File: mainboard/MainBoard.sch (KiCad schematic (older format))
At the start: 37 parts, among them J1 CONN_1x4, J2 CONN_2X3, J3 CONN_2X3, J5 SWDEBUG_CONNECTOR, J7 CONN_2X12, U1 Tex_DCDC

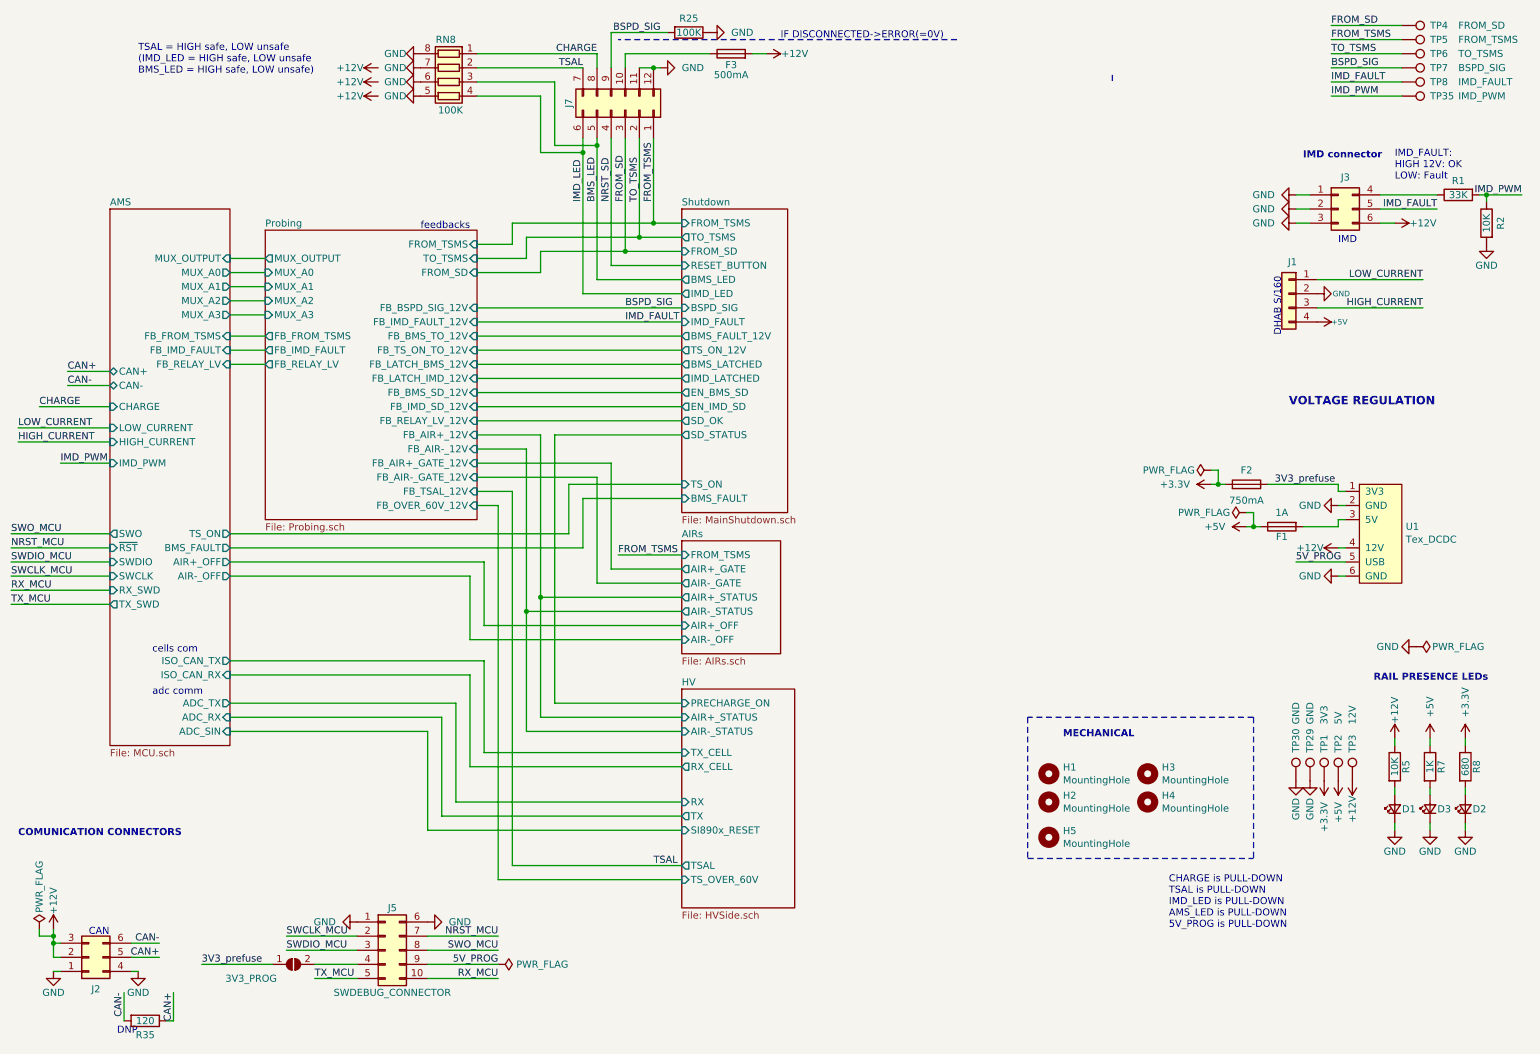
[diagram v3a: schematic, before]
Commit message: Renamed handcart detection
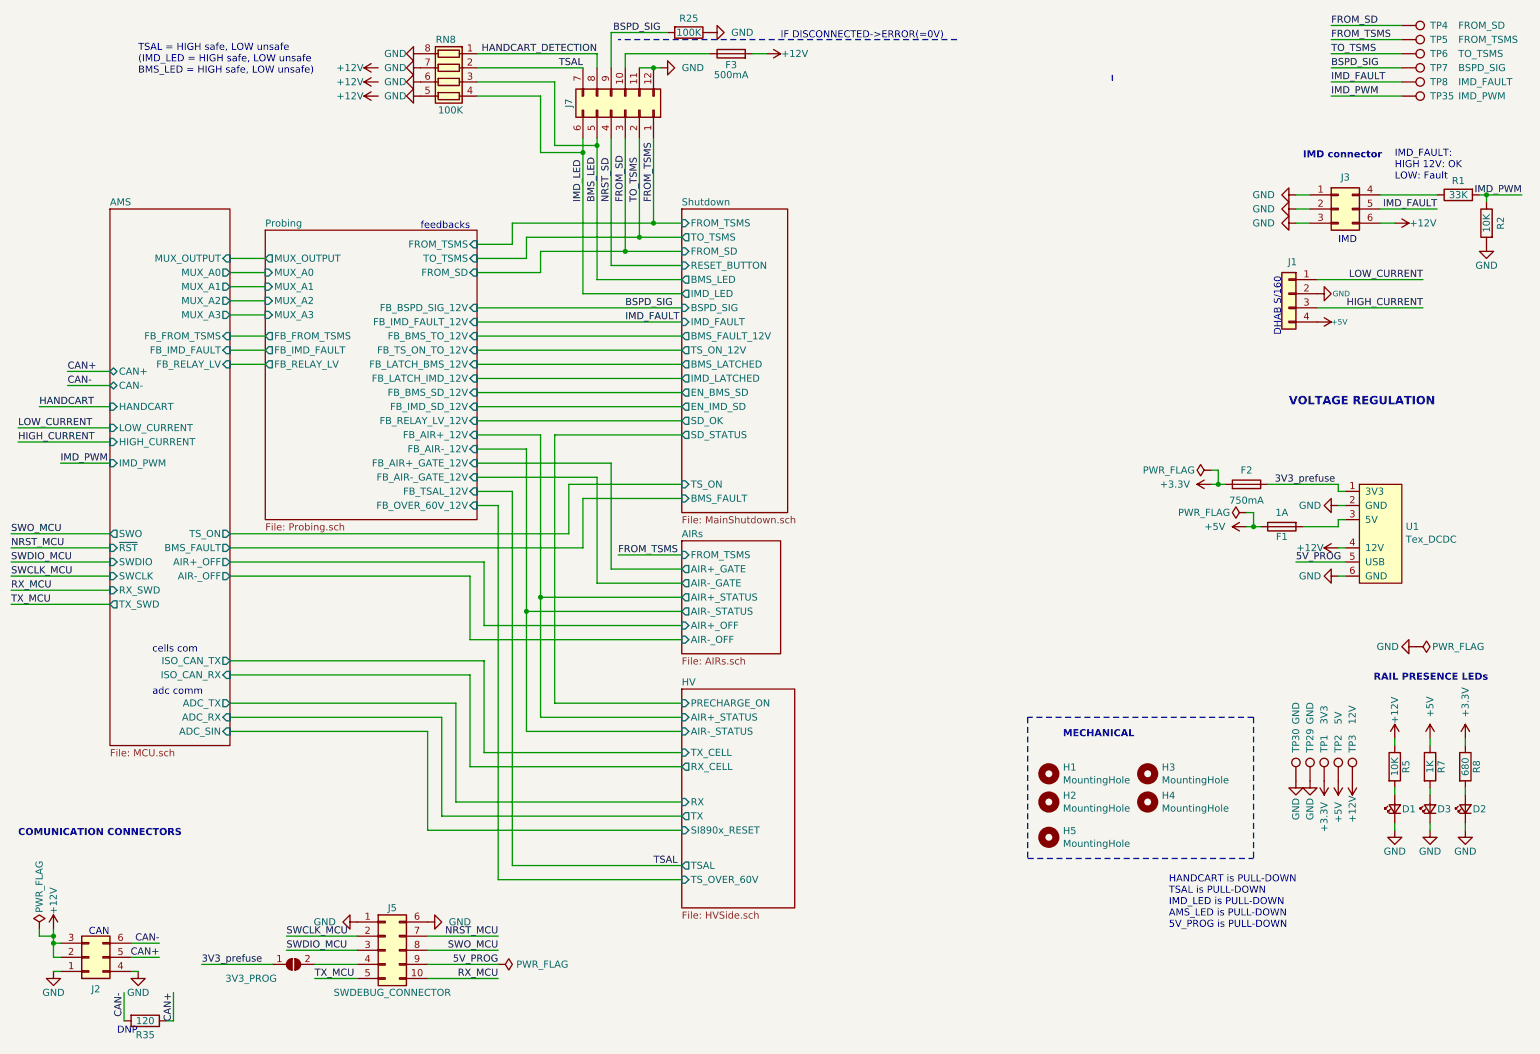
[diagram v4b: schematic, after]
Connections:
- net CHARGE renamed HANDCART_DETECTION
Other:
- note added: "HANDCART is PULL-DOWN\nTSAL is PULL-DOWN\nIMD_LED is PULL-DOWN\nAMS_LED is PULL-DOWN\n5V_PROG is PULL-DOWN"
- note removed: "CHARGE is PULL-DOWN\nTSAL is PULL-DOWN\nIMD_LED is PULL-DOWN\nAMS_LED is PULL-DOWN\n5V_PROG is PULL-DOWN"
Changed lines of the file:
@@
 F2 "HIGH_CURRENT" I L 1200 3550 50
 F3 "LOW_CURRENT" I L 1200 3450 50
-F4 "CHARGE" I L 1200 3300 50
+F4 "HANDCART" I L 1200 3300 50
 F5 "SWDIO" I L 1200 4400 50
 F6 "SWCLK" I L 1200 4500 50
@@
 BSPD_SIG
 Text Notes 8700 7000 0    50   ~ 0
-CHARGE is PULL-DOWN\nTSAL is PULL-DOWN\nIMD_LED is PULL-DOWN\nAMS_LED is PULL-DOWN\n5V_PROG is PULL-DOWN
+HANDCART is PULL-DOWN\nTSAL is PULL-DOWN\nIMD_LED is PULL-DOWN\nAMS_LED is PULL-DOWN\n5V_PROG is PULL-DOWN
 Text Label 4850 2700 0    50   ~ 0
 IMD_FAULT
@@
 	4950 1400 4950 2100
 Text Label 700  3300 0    50   ~ 0
-CHARGE
+HANDCART
 Wire Wire Line
 	700  3300 1200 3300
@@
 IMD_PWM
 Text Label 4650 800  2    50   ~ 0
-CHARGE
+HANDCART_DETECTION
 Wire Wire Line
 	5050 900  5100 900

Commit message: Correction almost finished, Started layouting
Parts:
- removed J1: CONN_1x4, MainBoard:Molex_Micro-Fit_3.0_43650-0415_1x04_P3.00mm_Vertical, symbol Connector_Generic:Conn_01x04
- removed R25: 100K, Resistor_SMD:R_0603_1608Metric, symbol Device:R
- removed R35: 120, Resistor_SMD:R_0805_2012Metric, symbol Device:R
- H1, H2, H3, H4, H5: footprint MountingHole:MountingHole_3mm -> Eagle_Main:MountingHole_3.2_6.1Free
- J2: value CONN_2X3 -> CAN_POWER; footprint MainBoard:Molex_Micro-Fit_3.0_43045-0612_2x03_P3.00mm_Vertical -> Connector_Molex:Molex_Micro-Fit_3.0_43045-0612_2x03_P3.00mm_Vertical
- J3: footprint MainBoard:Molex_Micro-Fit_3.0_43045-0612_2x03_P3.00mm_Vertical -> Connector_Molex:Molex_Micro-Fit_3.0_43045-0612_2x03_P3.00mm_Vertical
- J7: value CONN_2X12 -> SIGNALS_INOUT; footprint MainBoard:Molex_Micro-Fit_3.0_43045-1212_2x06_P3.00mm_Vertical -> Connector_Molex:Molex_Micro-Fit_3.0_43045-1212_2x06_P3.00mm_Vertical; symbol Connector_Generic:Conn_02x06_Counter_Clockwise -> Connector_Generic:Conn_02x06_Top_Bottom
- RN8: footprint MainBoard:R_network_4x1_bourns_CAY16 -> Resistor_SMD:R_Array_Convex_4x0603
- TP29, TP30: footprint MainBoard:TestPoint_GNDedge -> Eagle_Main:TestPoint_GNDedge
- TP4: value FROM_SD -> SD_IN
- TP5: value FROM_TSMS -> SD_END
- TP6: value TO_TSMS -> SD_OUT
- TP7: value BSPD_SIG -> EXT_FAULT
- U1: footprint MainBoard:Tex_DCDC_vertical -> Eagle_Main:Tex_DCDC_vertical_up; symbol MainBoard:Tex_DCDC -> Eagle_Main:Tex_DCDC
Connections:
- net GND: now also J7.7 (Pin_7), J7.8 (Pin_8); no longer J7.11 (Pin_11), J7.12 (Pin_12)
- net HANDCART_DETECTION: now also J7.9 (Pin_9); no longer J7.8 (Pin_8)
- net TSAL: now also J7.11 (Pin_11); no longer J7.7 (Pin_7)
- net EXT_FAULT: now reaches J7.10 (Pin_10)
- net EXT_FAULT: now also TP7.1; no longer F3.1
- net BMS_LED renamed BMS_COCKPIT
- net BMS_COCKPIT: now also RN8.4 (R4.1); no longer RN8.3 (R3.1)
- removed net BSPD_SIG: J7.9 (Pin_9), TP7.1
- net FROM_SD renamed SD_IN
- net FROM_TSMS renamed SD_END
- net IMD_LED renamed IMD_COCKPIT
- net IMD_COCKPIT: now also RN8.3 (R3.1); no longer RN8.4 (R4.1)
- net NRST_SD renamed SD_RESET
- net TO_TSMS renamed SD_OUT
- new net TSAL_12V: F3.1, J7.12 (Pin_12)
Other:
- note added: "HANDCART is PULL-DOWN\nTSAL is PULL-DOWN\nIMD_COCKPIT is PULL-DOWN\nAMS_LED is PULL-DOWN\n5V_PROG is PULL-DOWN"
- note added: "TSAL = HIGH safe, LOW unsafe\n(IMD_COCKPIT = HIGH safe, LOW fault\nBMS_COCKPIT = HIGH safe, LOW fault)"
- note removed: "CAN"
- note removed: "DHAB S/160"
- note removed: "DNP"
- note removed: "HANDCART is PULL-DOWN\nTSAL is PULL-DOWN\nIMD_LED is PULL-DOWN\nAMS_LED is PULL-DOWN\n5V_PROG is PULL-DOWN"
- note removed: "IF DISCONNECTED->ERROR(=0V)"
- note removed: "TSAL = HIGH safe, LOW unsafe\n(IMD_LED = HIGH safe, LOW unsafe\nBMS_LED = HIGH safe, LOW unsafe)"
- note removed: "feedbacks"
- moved on the sheet: F1, F3, J5, RN8
